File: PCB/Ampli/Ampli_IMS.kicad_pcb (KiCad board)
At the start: 2 copper layers, 44.4 x 32 mm, 15 parts, among them J1 5227161-3, J2 5227161-3, J3 Conn_01x03_Male, P1 300K, U1 LMC6082

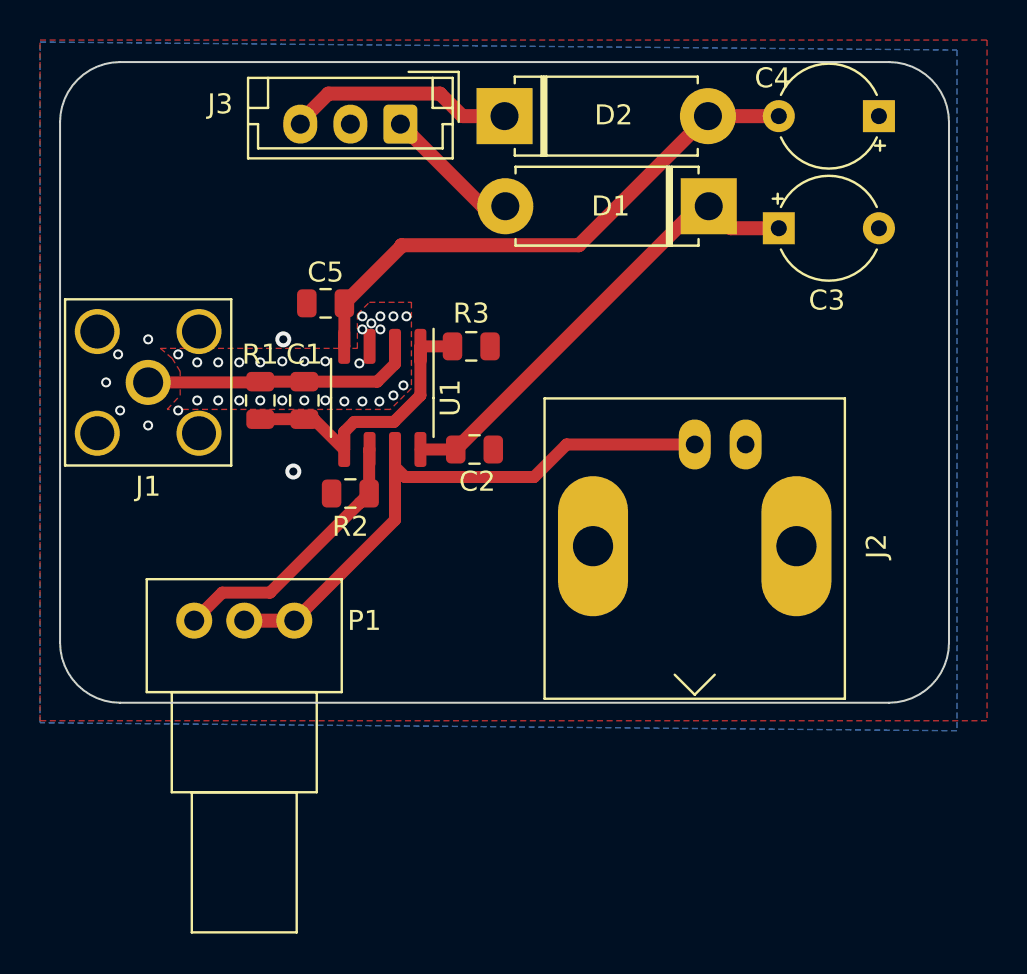
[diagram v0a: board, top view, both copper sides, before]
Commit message: Small mistakes
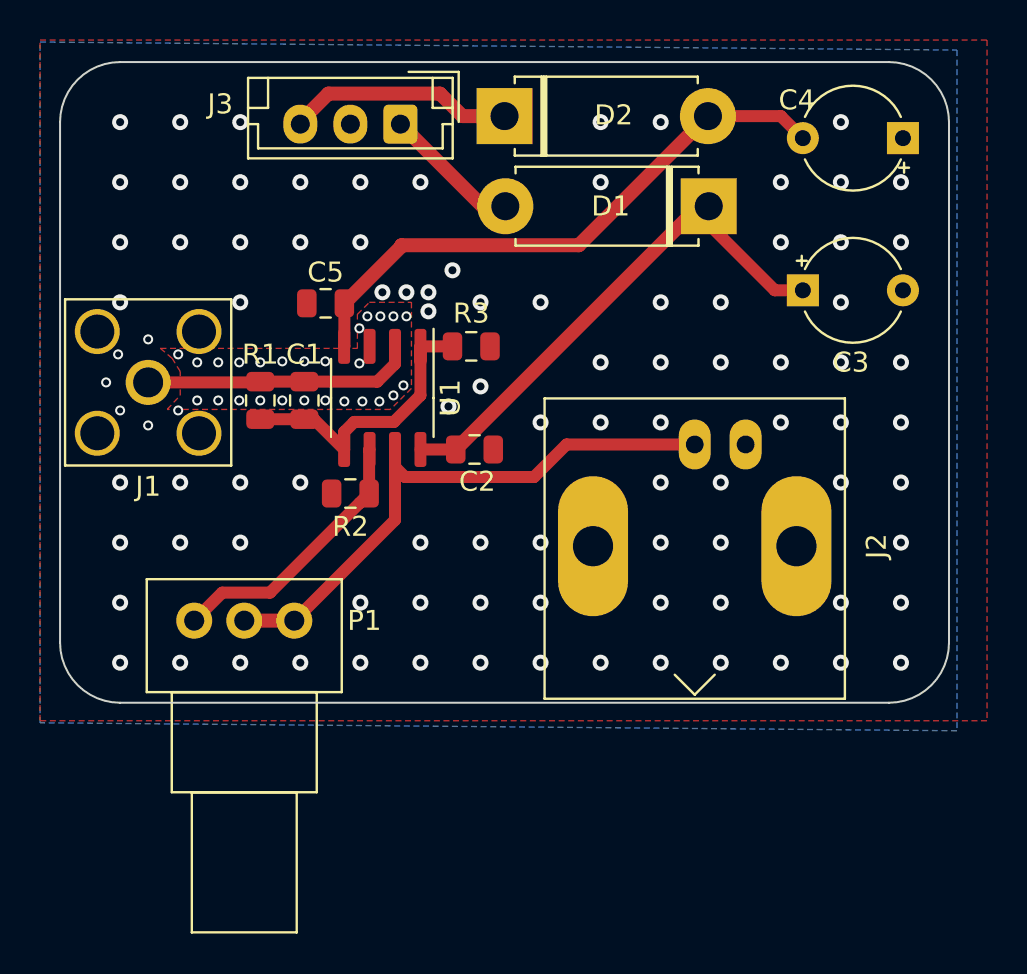
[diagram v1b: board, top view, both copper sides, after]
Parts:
- moved C3 3.32 mm to (61.7, 29.4)
- moved C4 1.63 mm to (66.7, 21.8)
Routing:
- net /+5V: track 23.4 -> 26.4 mm
- net /-5V: track 27.8 -> 29.4 mm
- net GND: vias 36 -> 122

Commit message: Improve PCBs
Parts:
- C3, C4: footprint Capacitor_THT:CP_Radial_Tantal_D5.0mm_P5.00mm -> Capacitor_Tantalum_SMD:CP_EIA-3216-18_Kemet-A_Pad1.58x1.35mm_HandSolder
- D1, D2: footprint Diode_THT:D_5W_P10.16mm_Horizontal -> Diode_SMD:D_0805_2012Metric_Castellated
- moved J3 19.7 mm to (61.0, 24.5)
- moved C4 14.5 mm to (54.4, 29.5)
- moved D2 9.90 mm to (54.0, 27.5), turned to 180 degrees
- moved D1 4.19 mm to (60.5, 27.5), turned to 0 degrees
- moved C3 0.77 mm to (60.9, 29.5)
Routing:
- net /-5V: track 29.4 -> 18.6 mm
- net Net-(D2-Pad1): track 11.4 -> 3.43 mm
- net /+5V: track 26.4 -> 22.4 mm
- net Net-(D1-Pad2): track 6.94 -> 3.19 mm
- net GND: vias 122 -> 218
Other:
- board size 44.4 x 32 mm -> 44.4 x 28.5 mm

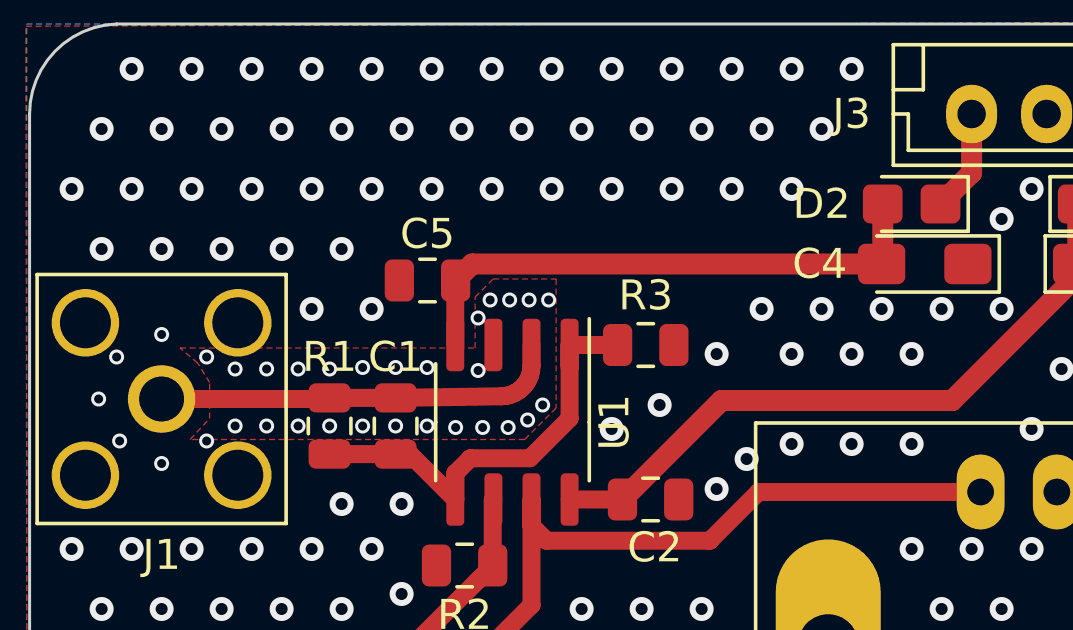
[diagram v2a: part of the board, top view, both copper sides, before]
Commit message: Ampli last version - low noise guarding
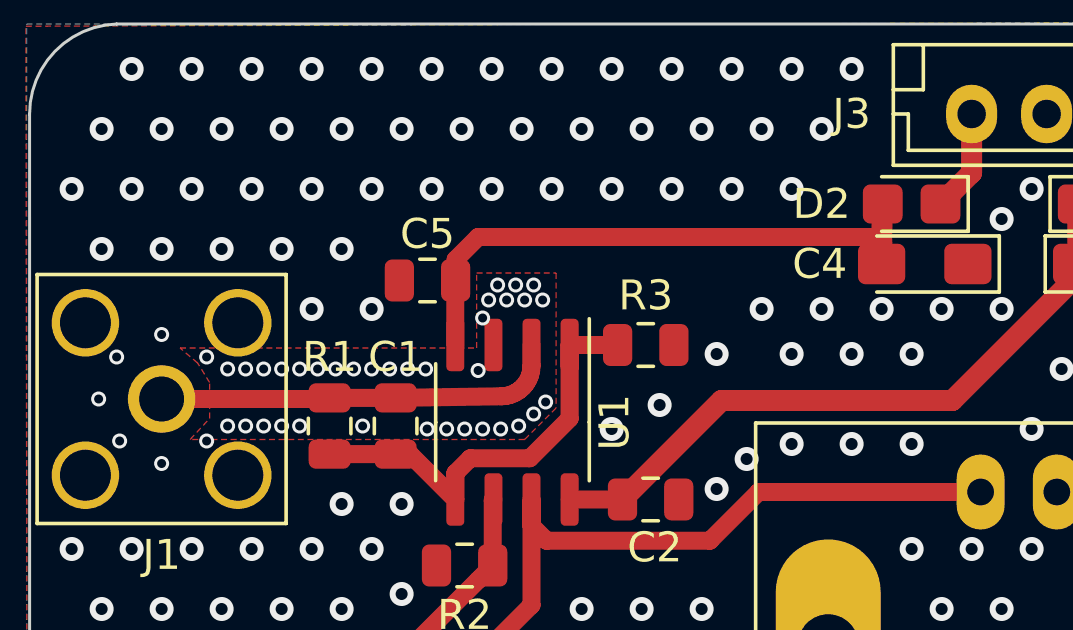
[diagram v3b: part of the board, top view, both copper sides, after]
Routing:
- net /-5V: track 18.6 -> 19.4 mm
- net GND: vias 218 -> 228
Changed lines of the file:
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@@
     (thickness 1.6)
     (drawings 11)
-    (tracks 275)
+    (tracks 287)
     (zones 0)
     (modules 15)
@@
     (34 B.Paste user hide)
     (35 F.Paste user)
-    (36 B.SilkS user)
+    (36 B.SilkS user hide)
     (37 F.SilkS user)
-    (38 B.Mask user)
-    (39 F.Mask user hide)
+    (38 B.Mask user hide)
+    (39 F.Mask user)
     (40 Dwgs.User user)
     (41 Cmts.User user)
@@
   )
   (setup
-    (last_trace_width 0.6)
+    (last_trace_width 0.25)
     (user_trace_width 0.2)
     (user_trace_width 0.4)
@@
   (gr_line (start 65.9 21.5) (end 27.5 21.5) (layer Edge.Cuts) (width 0.1))
   (gr_line (start 27.6 50) (end 66 50) (layer Edge.Cuts) (width 0.1))
-  (via (at 41.2 34.7) (size 0.5) (drill 0.3) (layers F.Cu B.Cu) (net 1))
-  (via (at 41.7 34.2) (size 0.5) (drill 0.3) (layers F.Cu B.Cu) (net 1))
+  (via (at 32.4 34.9) (size 0.5) (drill 0.3) (layers F.Cu B.Cu) (net 1))
+  (via (at 33 34.9) (size 0.5) (drill 0.3) (layers F.Cu B.Cu) (net 1))
+  (via (at 38.5 35) (size 0.5) (drill 0.3) (layers F.Cu B.Cu) (net 1))
+  (via (at 39.7 35) (size 0.5) (drill 0.3) (layers F.Cu B.Cu) (net 1))
+  (via (at 40.9 34.9) (size 0.5) (drill 0.3) (layers F.Cu B.Cu) (net 1))
+  (via (at 41.8 34.1) (size 0.5) (drill 0.3) (layers F.Cu B.Cu) (net 1))
   (via (at 42 47) (size 0.8) (drill 0.4) (layers F.Cu B.Cu) (net 1))
   (via (at 44 47) (size 0.8) (drill 0.4) (layers F.Cu B.Cu) (net 1))
@@
   (via (at 49 31) (size 0.8) (drill 0.4) (layers F.Cu B.Cu) (net 1))
   (via (at 47.5 32.5) (size 0.8) (drill 0.4) (layers F.Cu B.Cu) (net 1))
-  (via (at 32.5 34.9) (size 0.5) (drill 0.3) (layers F.Cu B.Cu) (net 1))
-  (via (at 32.5 33) (size 0.5) (drill 0.3) (layers F.Cu B.Cu) (net 1))
-  (via (at 40.6 30.7) (size 0.5) (drill 0.3) (layers F.Cu B.Cu) (net 1))
-  (via (at 35.7 32.95) (size 0.5) (drill 0.3) (layers F.Cu B.Cu) (net 1))
-  (via (at 36.8 32.95) (size 0.5) (drill 0.3) (layers F.Cu B.Cu) (net 1))
-  (via (at 40.55 34.95) (size 0.5) (drill 0.3) (layers F.Cu B.Cu) (net 1))
-  (via (at 38.8 34.95) (size 0.5) (drill 0.3) (layers F.Cu B.Cu) (net 1))
-  (via (at 36.8 34.9) (size 0.5) (drill 0.3) (layers F.Cu B.Cu) (net 1))
-  (via (at 34.6 34.9) (size 0.5) (drill 0.3) (layers F.Cu B.Cu) (net 1))
-  (via (at 33.55 34.9) (size 0.5) (drill 0.3) (layers F.Cu B.Cu) (net 1))
-  (via (at 31.45 34.9) (size 0.5) (drill 0.3) (layers F.Cu B.Cu) (net 1))
+  (via (at 31.8 34.9) (size 0.5) (drill 0.3) (layers F.Cu B.Cu) (net 1))
+  (via (at 31.8 33) (size 0.5) (drill 0.3) (layers F.Cu B.Cu) (net 1))
+  (via (at 40.5 30.7) (size 0.5) (drill 0.3) (layers F.Cu B.Cu) (net 1))
+  (via (at 35.4 33) (size 0.5) (drill 0.3) (layers F.Cu B.Cu) (net 1))
+  (via (at 36 33) (size 0.5) (drill 0.3) (layers F.Cu B.Cu) (net 1))
+  (via (at 41.4 34.5) (size 0.5) (drill 0.3) (layers F.Cu B.Cu) (net 1))
+  (via (at 39.1 35) (size 0.5) (drill 0.3) (layers F.Cu B.Cu) (net 1))
+  (via (at 33.6 34.9) (size 0.5) (drill 0.3) (layers F.Cu B.Cu) (net 1))
+  (via (at 31.2 34.9) (size 0.5) (drill 0.3) (layers F.Cu B.Cu) (net 1))
   (via (at 30.5 35.4) (size 0.5) (drill 0.3) (layers F.Cu B.Cu) (net 1))
   (via (at 29 36.15) (size 0.5) (drill 0.3) (layers F.Cu B.Cu) (net 1))
@@
   (via (at 29 31.85) (size 0.5) (drill 0.3) (layers F.Cu B.Cu) (net 1))
   (via (at 30.5 32.6) (size 0.5) (drill 0.3) (layers F.Cu B.Cu) (net 1))
-  (via (at 31.45 33) (size 0.5) (drill 0.3) (layers F.Cu B.Cu) (net 1))
-  (via (at 33.55 33) (size 0.5) (drill 0.3) (layers F.Cu B.Cu) (net 1))
-  (via (at 37.85 32.95) (size 0.5) (drill 0.3) (layers F.Cu B.Cu) (net 1))
-  (via (at 34.6 33) (size 0.5) (drill 0.3) (layers F.Cu B.Cu) (net 1))
+  (via (at 31.2 33) (size 0.5) (drill 0.3) (layers F.Cu B.Cu) (net 1))
+  (via (at 32.4 33) (size 0.5) (drill 0.3) (layers F.Cu B.Cu) (net 1))
+  (via (at 36.6 33) (size 0.5) (drill 0.3) (layers F.Cu B.Cu) (net 1))
+  (via (at 33 33) (size 0.5) (drill 0.3) (layers F.Cu B.Cu) (net 1))
   (via (at 35.7 34.9) (size 0.5) (drill 0.3) (layers F.Cu B.Cu) (net 1))
-  (via (at 37.85 34.9) (size 0.5) (drill 0.3) (layers F.Cu B.Cu) (net 1))
-  (via (at 39.7 34.95) (size 0.5) (drill 0.3) (layers F.Cu B.Cu) (net 1))
-  (via (at 39.95 30.7) (size 0.5) (drill 0.3) (layers F.Cu B.Cu) (net 1))
-  (via (at 41.25 30.7) (size 0.5) (drill 0.3) (layers F.Cu B.Cu) (net 1))
-  (via (at 39.55 31.3) (size 0.5) (drill 0.3) (layers F.Cu B.Cu) (net 1))
-  (via (at 41.9 30.7) (size 0.5) (drill 0.3) (layers F.Cu B.Cu) (net 1))
+  (via (at 37.85 35) (size 0.5) (drill 0.3) (layers F.Cu B.Cu) (net 1))
+  (via (at 40.3 35) (size 0.5) (drill 0.3) (layers F.Cu B.Cu) (net 1))
+  (via (at 39.9 30.7) (size 0.5) (drill 0.3) (layers F.Cu B.Cu) (net 1))
+  (via (at 41.1 30.7) (size 0.5) (drill 0.3) (layers F.Cu B.Cu) (net 1))
+  (via (at 39.7 31.3) (size 0.5) (drill 0.3) (layers F.Cu B.Cu) (net 1))
+  (via (at 41.7 30.7) (size 0.5) (drill 0.3) (layers F.Cu B.Cu) (net 1))
   (via (at 39.55 33.05) (size 0.5) (drill 0.3) (layers F.Cu B.Cu) (net 1))
   (via (at 45.6 34.2) (size 0.8) (drill 0.4) (layers F.Cu B.Cu) (net 1))
@@
   (via (at 39 49) (size 0.8) (drill 0.4) (layers F.Cu B.Cu) (net 1))
   (via (at 38 47) (size 0.8) (drill 0.4) (layers F.Cu B.Cu) (net 1))
+  (via (at 33.6 33) (size 0.5) (drill 0.3) (layers F.Cu B.Cu) (net 1))
+  (via (at 34.2 33) (size 0.5) (drill 0.3) (layers F.Cu B.Cu) (net 1))
+  (via (at 34.8 33) (size 0.5) (drill 0.3) (layers F.Cu B.Cu) (net 1))
+  (via (at 37.2 33) (size 0.5) (drill 0.3) (layers F.Cu B.Cu) (net 1))
+  (via (at 37.8 33) (size 0.5) (drill 0.3) (layers F.Cu B.Cu) (net 1))
+  (via (at 40.2 30.2) (size 0.5) (drill 0.3) (layers F.Cu B.Cu) (net 1))
+  (via (at 40.8 30.2) (size 0.5) (drill 0.3) (layers F.Cu B.Cu) (net 1))
+  (via (at 41.4 30.2) (size 0.5) (drill 0.3) (layers F.Cu B.Cu) (net 1))
   (segment (start 61.4625 24.9625) (end 61 24.5) (width 0.7) (layer F.Cu) (net 2))
   (segment (start 61.4625 27.5) (end 61.4625 24.9625) (width 0.7) (layer F.Cu) (net 2))
@@
   (segment (start 44.3625 37.35) (end 47.662501 34.049999) (width 0.7) (layer F.Cu) (net 4))
   (segment (start 53.0375 29.4625) (end 53 29.5) (width 0.7) (layer F.Cu) (net 5))
-  (segment (start 53.0375 27.5) (end 53.0375 29.4625) (width 0.7) (layer F.Cu) (net 5))
   (segment (start 38.79 30.06) (end 38.8 30.05) (width 0.6) (layer F.Cu) (net 5))
   (segment (start 38.79 32.2) (end 38.79 30.06) (width 0.6) (layer F.Cu) (net 5))
-  (segment (start 39.35 29.5) (end 53 29.5) (width 0.7) (layer F.Cu) (net 5))
-  (segment (start 38.8 30.05) (end 39.35 29.5) (width 0.7) (layer F.Cu) (net 5))
+  (segment (start 38.8 29.35) (end 39.55 28.6) (width 0.6) (layer F.Cu) (net 5))
+  (segment (start 38.8 30.05) (end 38.8 29.35) (width 0.6) (layer F.Cu) (net 5))
+  (segment (start 39.55 28.6) (end 53 28.6) (width 0.6) (layer F.Cu) (net 5))
+  (segment (start 53 28.6) (end 53.0375 29.4625) (width 0.7) (layer F.Cu) (net 5))
+  (segment (start 53.0375 27.5) (end 53 28.6) (width 0.7) (layer F.Cu) (net 5))
   (segment (start 34.5625 34) (end 34.6 33.9625) (width 0.6) (layer F.Cu) (net 6))
   (segment (start 29 34) (end 34.5625 34) (width 0.6) (layer F.Cu) (net 6))
@@
     (polygon
       (pts
-        (xy 42.1 34.35) (xy 41.1 35.35) (xy 30 35.35) (xy 30.65 34.55) (xy 31.05 34.55)
-        (xy 40.65 34.5) (xy 41.85 33.25) (xy 41.85 31.1) (xy 40.85 31.1) (xy 40.85 32.85)
+        (xy 42.1 34.35) (xy 41.1 35.3) (xy 37.7 35.3) (xy 37.5 34.9) (xy 37.7 34.5)
+        (xy 40.8 34.5) (xy 41.9 33.275) (xy 41.9 31.1) (xy 40.5 31.1) (xy 40.5 32.85)
         (xy 40.225 33.45) (xy 30.775 33.45) (xy 30 32.55) (xy 38.3 32.55) (xy 38.29375 33.05)
-        (xy 38.425 33.25) (xy 39.15 33.25) (xy 39.3 32.95) (xy 39.3 32.3) (xy 39.45 32.3)
-        (xy 39.45 30.6) (xy 39.9 30.15) (xy 42.1 30.15)
+        (xy 38.425 33.25) (xy 39.2 33.25) (xy 39.5 32.6) (xy 39.5 32.3) (xy 39.5 29.9)
+        (xy 42.1 29.9)
       )
     )
@@
       (pts
         (xy 42.15 34.3) (xy 41.1 35.35) (xy 29.95 35.35) (xy 30.6 34.65) (xy 30.6 33.45)
-        (xy 30.2 32.8) (xy 29.6125 32.3) (xy 39.45 32.3) (xy 39.45 30.6) (xy 40.05 30)
-        (xy 42.15 30)
+        (xy 30.2 32.8) (xy 29.6125 32.3) (xy 39.5 32.3) (xy 39.5 29.8) (xy 42.15 29.8)
       )
     )
+  )
+  (zone (net 0) (net_name "") (layer F.Mask) (hatch edge 0.508)
+    (connect_pads (clearance 0.508))
+    (min_thickness 0.254)
+    (fill yes (arc_segments 32) (thermal_gap 0.508) (thermal_bridge_width 0.508))
+    (polygon
+      (pts
+        (xy 34 34.9) (xy 33.7 35.3) (xy 30.1 35.3) (xy 30.7 34.5) (xy 33.7 34.5)
+      )
+    )
+  )
+  (zone (net 0) (net_name "") (layer F.Mask) (hatch edge 0.508)
+    (connect_pads (clearance 0.508))
+    (min_thickness 0.254)
+    (fill yes (arc_segments 32) (thermal_gap 0.508) (thermal_bridge_width 0.508))
+    (polygon
+      (pts
+        (xy 36.1 34.9) (xy 35.9 35.3) (xy 35.5 35.3) (xy 35.3 34.9) (xy 35.5 34.5)
+        (xy 35.9 34.5)
+      )
+    )
